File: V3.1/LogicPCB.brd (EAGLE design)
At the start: 171.9 x 151.6 mm, 65 parts, among them CON1 CUBE_ORANGE_, CON10 PINHEAD_1X02-2.54, CON11 CON-4P-JST-XA, CON12 PINHEAD_1X06-2.54, CON13 CON-6P-JST-XA, CON14 PINHEAD_1X04-2.54, CON15 CON-4P-JST-XA, CON17 CON-4P-JST-XA, CON18 CON-6P-JST-XA, CON19 USB-TYPE-C-VERT-PROD, CON2 CON-4P-JST-XA, CON20 PINHEAD_1X06-2.54, CON21 CON-4P-JST-XA, CON22 CON-4P-JST-XA, CON23 CON-4P-JST-XA, CON24 CON-4P-JST-XA, CON25 CON-4P-JST-XA, CON26 CON-4P-JST-XA, CON27 CON-4P-JST-XA, CON28 CON-4P-JST-XA, CON29 CON-4P-JST-XA, CON3 RJ45-NO_SHIELD-5556416-1, CON30 CON-4P-JST-XA, CON32 CON-4P-JST-XA, CON35 CON-12P-JST-XA, CON4 CON-2P-JST-XA, CON5 CON-6P-JST-XA, CON6 CON-4P-JST-XA, CON7 PINHEAD_1X06-2.54, CON9 PINHEAD_1X12-2.54, IC5 AOZ1280, M1 05G_ETHERNET_SWITCH, Q1 IRLML0030, T1 H1102NL, T2 H1102NL, T3 H1102NL, T4 H1102NL

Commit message: uarts
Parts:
- added R4, R5: (no value), rc:R0603
- added R6, R7: 000, rc:R0603
- moved R1 0.20 mm to (8.70, -26.3)
- moved R3 0.20 mm to (8.70, -24.7)
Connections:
- new net N$10: CON18.4, R5.1
- new net N$9: CON18.3, R4.1
- net GND: no longer CON35.10
- net HLK_RX0: now also CON35.6
- net HLK_RX1: now also R6.1
- net HLK_TX0: now also CON35.5
- net HLK_TX1: now also R7.1
- net SERIAL1_RX: now also R5.2, R7.2; no longer CON18.4
- net SERIAL1_TX: now also R4.2, R6.2; no longer CON18.3
- net SERIAL3_RX: now also CON35.8; no longer CON35.6
- net SERIAL3_TX: now also CON35.7; no longer CON35.5
- net VDD_24V: now also CON35.10; no longer CON35.7, CON35.8
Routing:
- net HLK_RX0: track 0.00 -> 81.8 mm, vias 0 -> 2
- net HLK_TX0: track 0.00 -> 76.3 mm, vias 0 -> 2
- net HLK_TX1: track 0.00 -> 43.1 mm, vias 0 -> 2
- net HLK_RX1: track 0.00 -> 39.6 mm, vias 0 -> 2
- net N$9: track 0.00 -> 13.9 mm
- net N$10: track 0.00 -> 12.1 mm
- net SERIAL1_TX: track 133.7 -> 124.0 mm
- net SERIAL1_RX: track 132.5 -> 123.1 mm
- net SERIAL3_RX: track 121.4 -> 116.5 mm
- net SERIAL3_TX: track 123.7 -> 118.8 mm
- net ETH1_RX-: track 35.4 -> 38.4 mm
- net VDD_24V: track 59.0 -> 56.5 mm
- net ETH1_RX+: track 36.6 -> 38.9 mm
- net GND: vias 114 -> 112
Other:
- board text added: "HLK0_RX"
- board text added: "HLK0_TX"
- board text added: "SER3_RX"
- board text removed: "SER_RX"

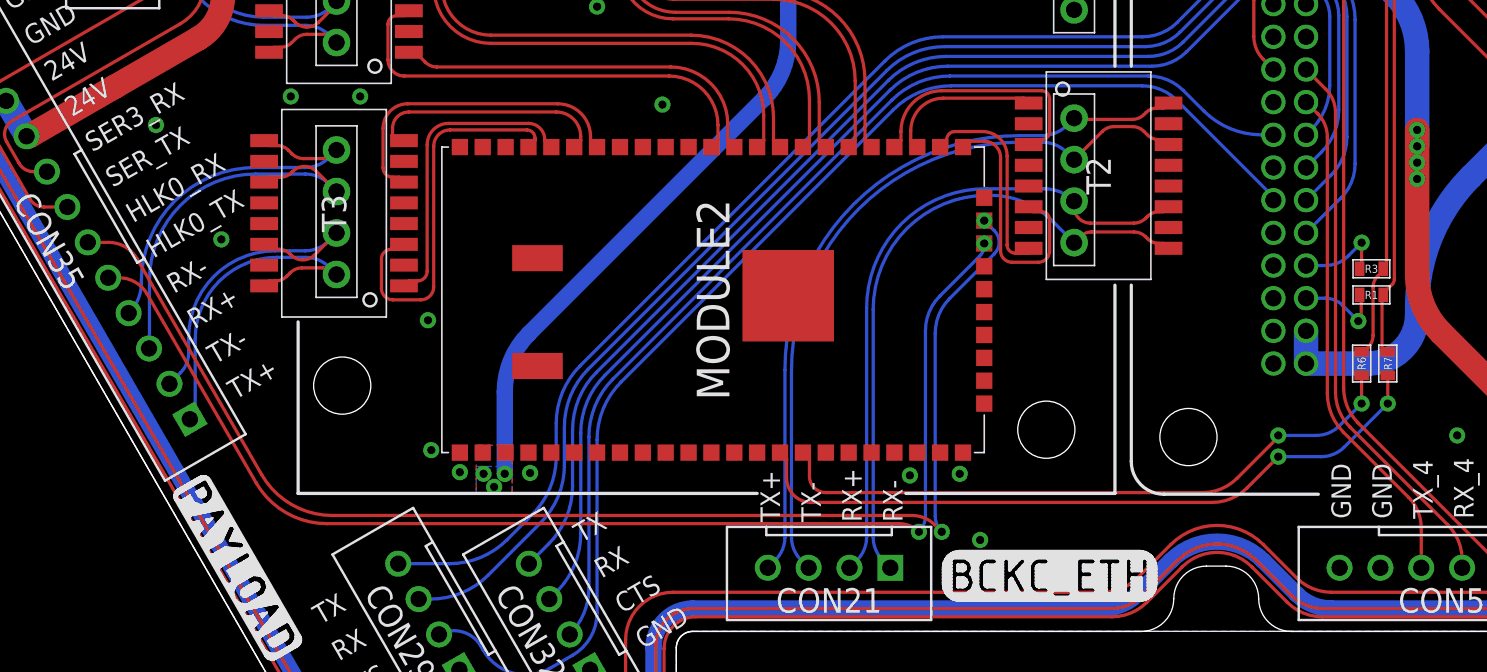
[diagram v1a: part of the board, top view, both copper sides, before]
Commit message: link leds added
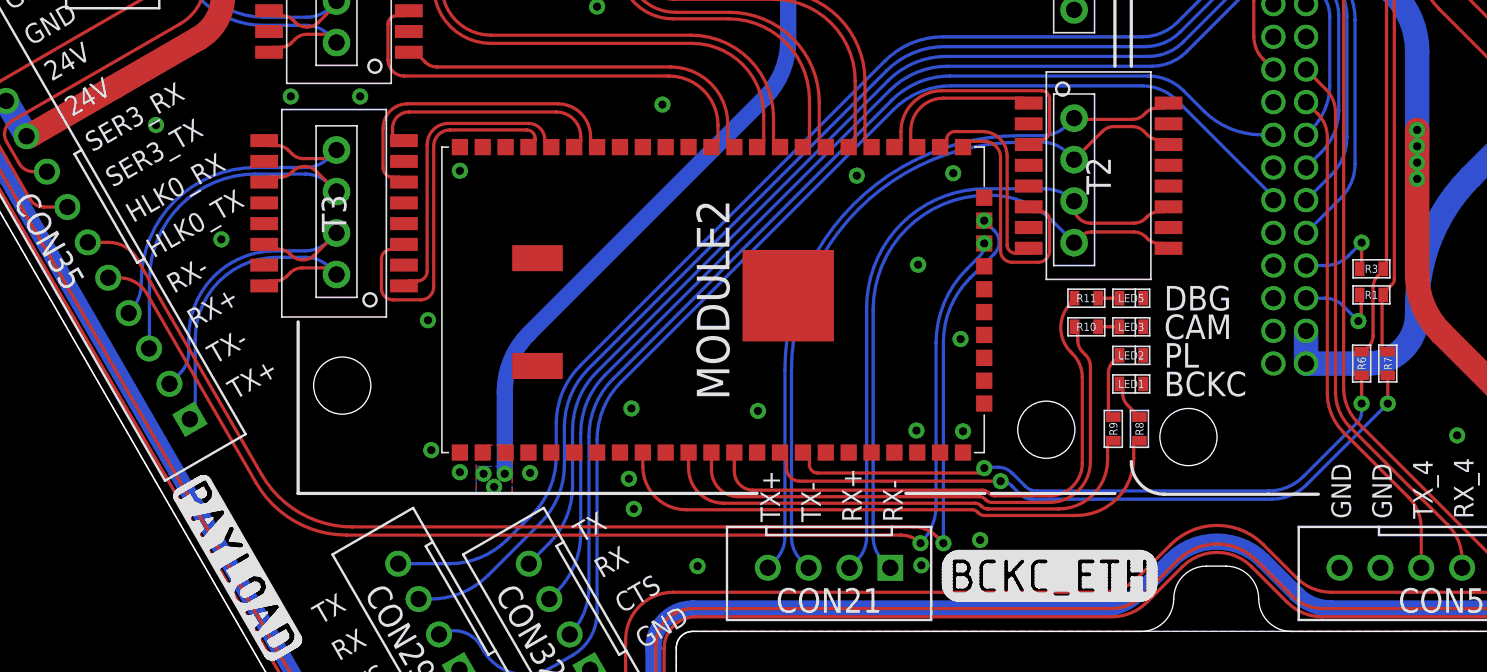
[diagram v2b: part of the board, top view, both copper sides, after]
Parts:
- added LED1, LED2, LED3, LED5: LED-0603, rc:LED0603
- added R10, R11, R8, R9: (no value), rc:R0603
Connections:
- removed net LINK0: MODULE2.13
- removed net LINK1: MODULE2.12
- new net N$11: LED1.A, R8.1
- new net N$12: LED2.A, R9.1
- new net N$14: LED3.A, R10.1
- new net N$15: LED5.A, R11.1
- new net N$16: MODULE2.12, R10.2
- new net N$17: MODULE2.13, R11.2
- net GND: now also LED1.C, LED2.C, LED3.C, LED5.C
- net LINK2: now also R9.2
- net LINK4: now also R8.2
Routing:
- net LINK4: track 0.00 -> 35.0 mm
- net N$16: track 0.00 -> 34.6 mm
- net N$17: track 0.00 -> 34.2 mm
- net LINK2: track 0.00 -> 30.3 mm
- net N$12: track 0.00 -> 4.29 mm
- net N$11: track 0.00 -> 2.47 mm
- net N$15: track 0.00 -> 1.30 mm
- net N$14: track 0.00 -> 1.30 mm
- net HLK_TX0: track 76.3 -> 76.9 mm
- net HLK_RX0: track 81.8 -> 82.4 mm
- net HLK_TX1: track 43.1 -> 42.5 mm
- net GND: vias 112 -> 123
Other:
- board text added: "BCKC"
- board text added: "CAM"
- board text added: "DBG"
- board text added: "PL"
- board text added: "SER3_TX"
- board text removed: "SER_TX"

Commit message: Naming
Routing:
- net BATT_CURRENT: track 54.9 -> 56.0 mm
- net SERIAL1_RX: track 123.1 -> 122.4 mm
- net SERIAL1_TX: track 124.0 -> 123.3 mm
- net ALARM: track 33.9 -> 34.5 mm
- net GND: vias 123 -> 126

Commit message: attribute updates
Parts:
- added D2, D3: ESDA5V3L, TVS_diodes:SOT23B-3
- added PAD1, PAD2: PAD-HEX-2MM, PADS:HEX-2MM
- added R12, R14, R15: 120R, rc:R0603
- D1: value MBR0520L-SOD123 -> SS34; device Diodes:SOD123 -> Diodes:DO-214AC(SMA)
- R1, R3, R6, R7: value 000 -> 120R
- R10, R11, R8, R9: value (none) -> 1K
- R16: value 10K -> 51K
- R20: value 200R -> 120R
- R35, R36, R37, R38: value 100R -> 120R
- R4, R5: value (none) -> 120R
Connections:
- new net N$18: CON18.5, R12.1
- net GND: now also D2.3, D3.3
- net HLK_RX0: now also R14.1
- net HLK_TX0: now also R15.1
- net PPM-SBUS-PROT: now also D3.1, R12.2; no longer CON18.5
- net RX_2: now also R14.2
- net SERIAL1_RX: now also D2.1
- net SERIAL1_TX: now also D2.2
- net TX_2: now also R15.2
- net USB_DM: now also PAD2.1
- net USB_DP: now also PAD1.1
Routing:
- net N$18: track 0.00 -> 10.4 mm
- net PPM-SBUS-PROT: track 81.2 -> 71.0 mm
- net RX_2: track 88.6 -> 98.1 mm
- net TX_2: track 91.9 -> 99.8 mm
- net USB_DP: track 0.00 -> 2.52 mm, vias 0 -> 1
- net USB_DM: track 0.00 -> 2.52 mm, vias 0 -> 1
- net HLK_TX0: track 76.9 -> 76.3 mm
- net HLK_RX0: track 82.4 -> 81.8 mm
- net GND: vias 126 -> 128
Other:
- board text added: "CON200"

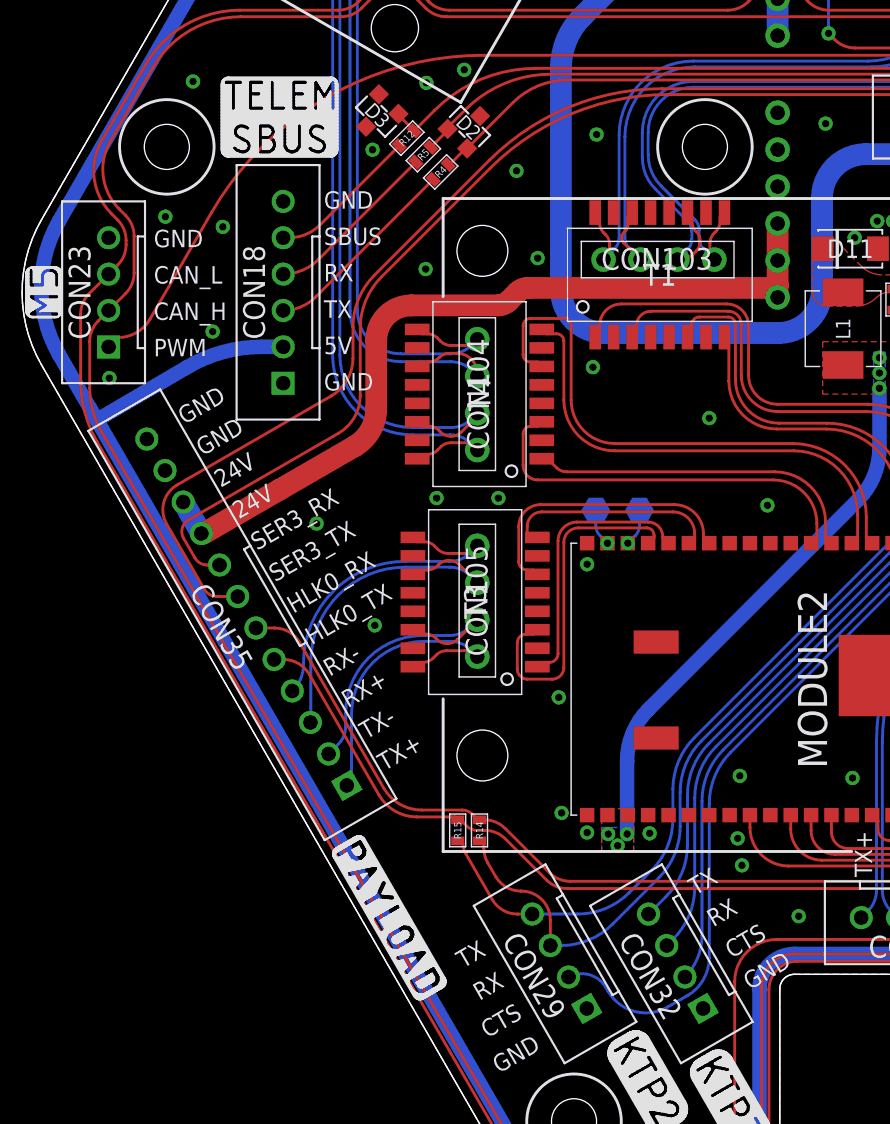
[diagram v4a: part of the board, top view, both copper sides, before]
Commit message: Payload connector replaced with 2 6-pin ones
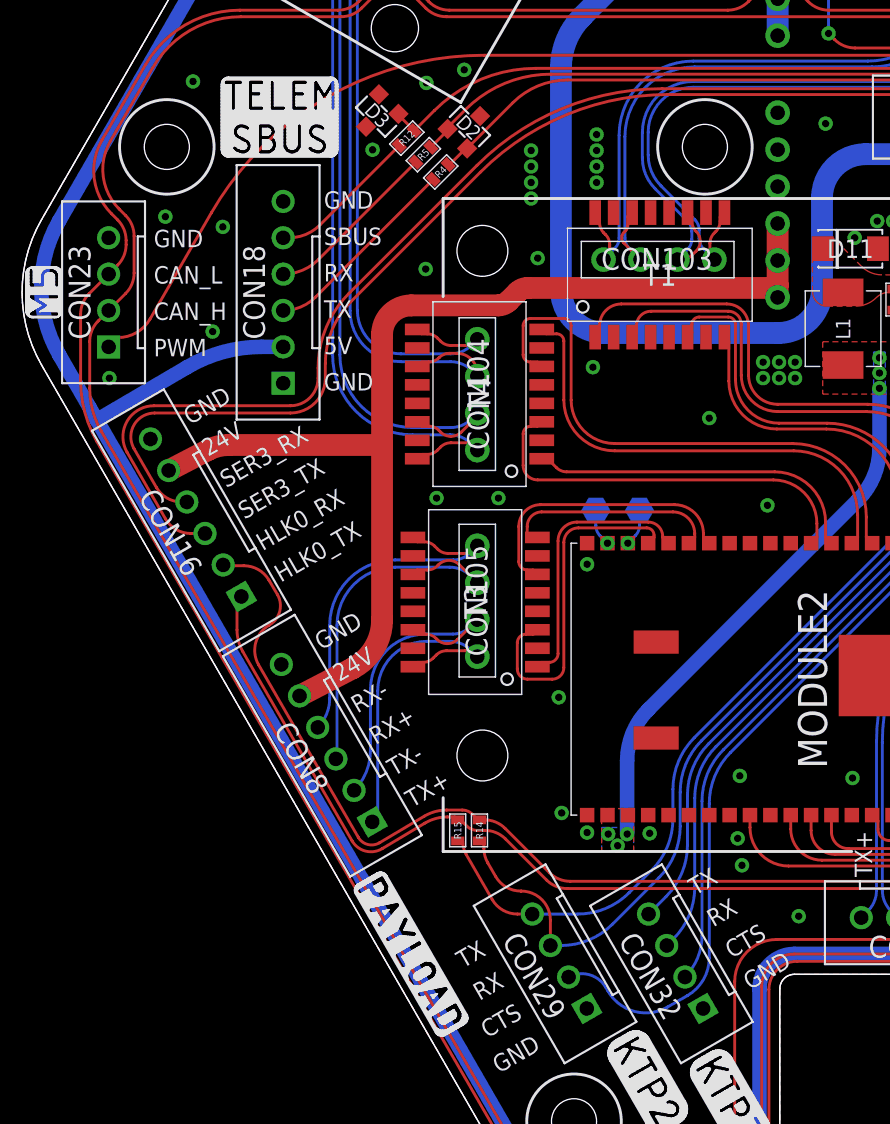
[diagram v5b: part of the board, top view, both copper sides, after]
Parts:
- removed CON35: CON-12P-JST-XA, Connectors:B12B-XASK-1
- added CON16, CON8: CON-6P-JST-XA, Connectors:B06B-XASK-1
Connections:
- net ETH5_RX+: now also CON8.3; no longer CON35.3
- net ETH5_RX-: now also CON8.4; no longer CON35.4
- net ETH5_TX+: now also CON8.1; no longer CON35.1
- net ETH5_TX-: now also CON8.2; no longer CON35.2
- net GND: now also CON16.6, CON8.6; no longer CON35.11, CON35.12
- net HLK_RX0: now also CON16.2; no longer CON35.6
- net HLK_TX0: now also CON16.1; no longer CON35.5
- net SERIAL3_RX: now also CON16.4; no longer CON35.8
- net SERIAL3_TX: now also CON16.3; no longer CON35.7
- net VDD_24V: now also CON16.5, CON8.5; no longer CON35.10, CON35.9
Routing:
- net VDD_24V: track 56.5 -> 76.3 mm
- net HLK_RX0: track 81.8 -> 92.2 mm
- net HLK_TX0: track 76.3 -> 85.1 mm
- net ETH5_RX-: track 22.2 -> 24.4 mm
- net ETH5_RX+: track 23.8 -> 26.0 mm
- net ETH5_TX+: track 20.9 -> 22.6 mm
- net ETH5_TX-: track 20.0 -> 21.6 mm
- net SERIAL3_RX: track 116.8 -> 118.1 mm
- net SERIAL3_TX: track 119.0 -> 119.9 mm
- net GND: vias 128 -> 138

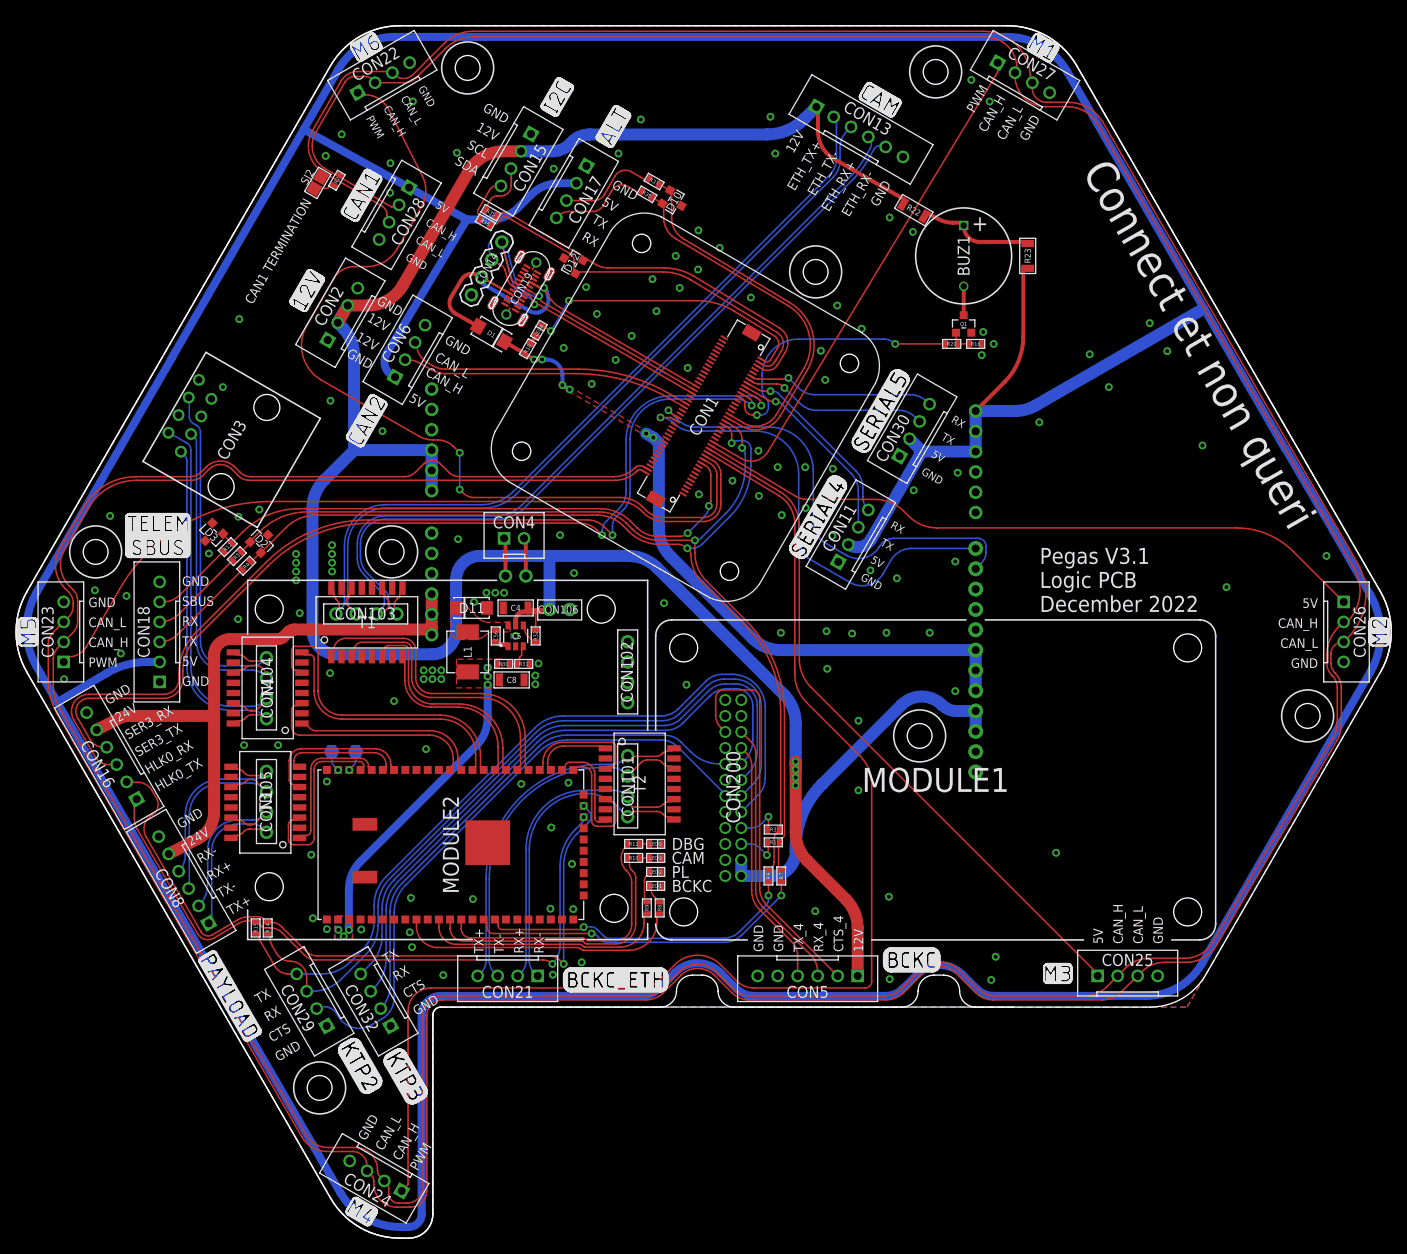
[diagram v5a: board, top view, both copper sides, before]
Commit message: InterPCB connectors issues fix
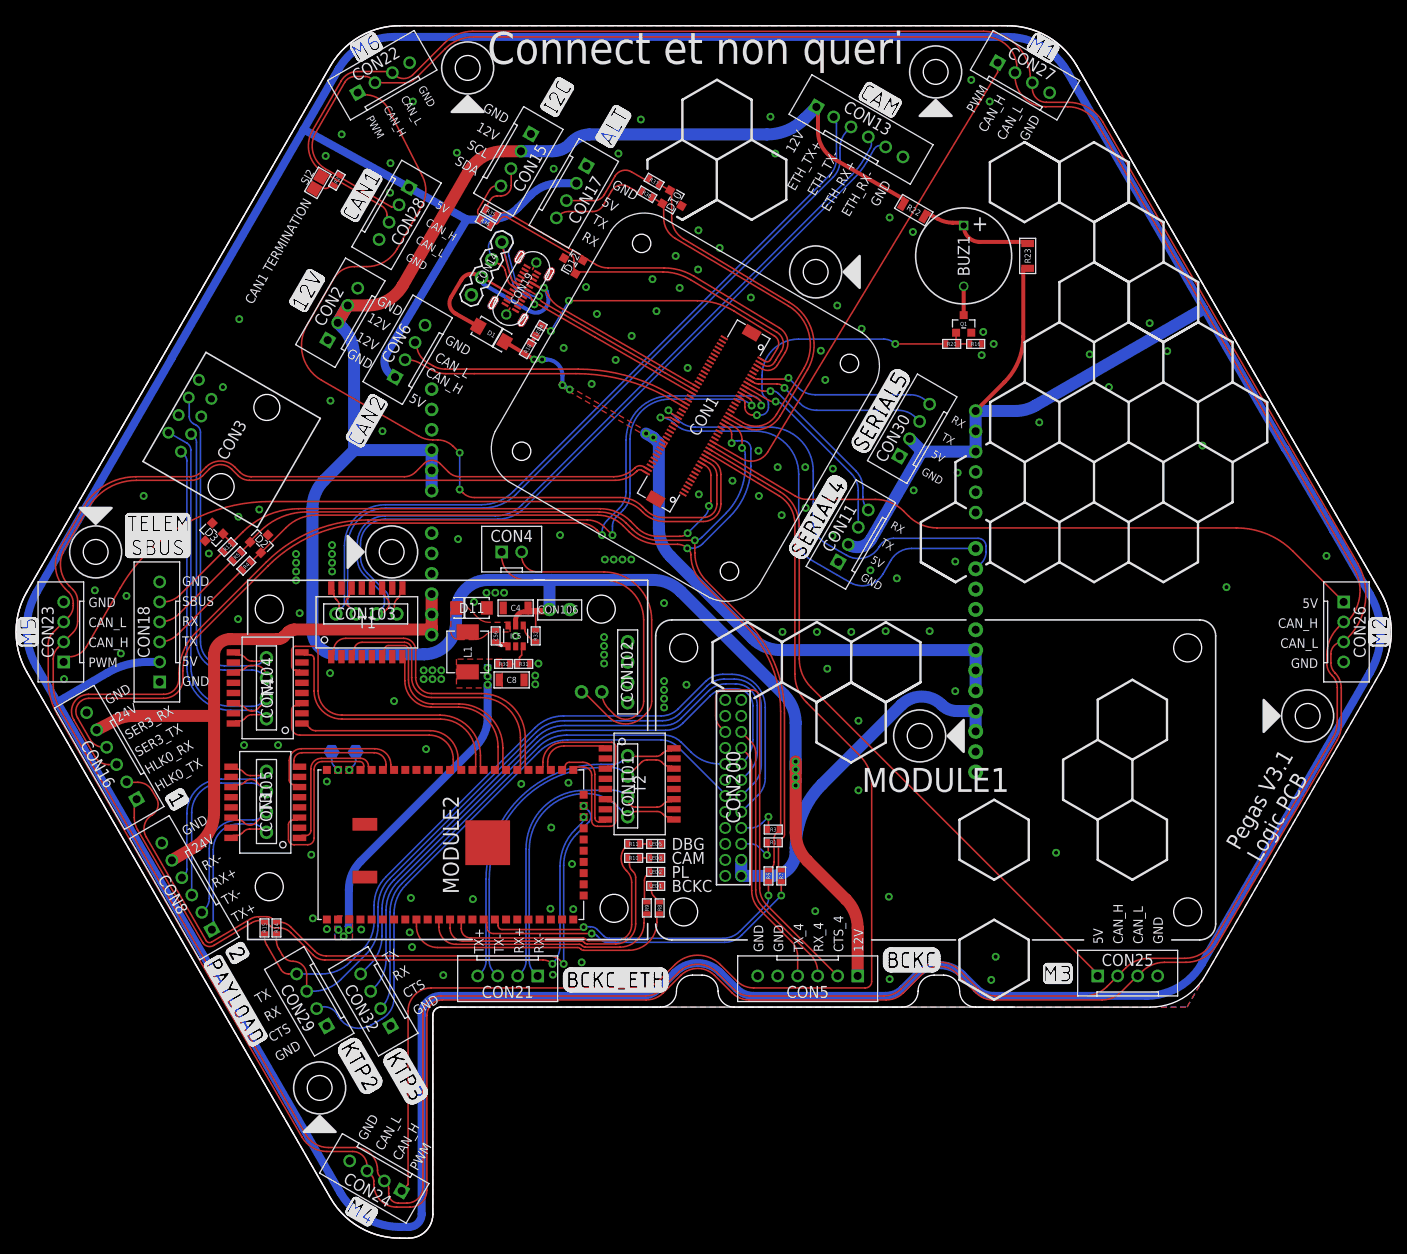
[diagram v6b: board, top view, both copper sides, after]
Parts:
- moved CON10 17.3 mm to (-14.0, -7.50), turned to 0 degrees
- moved CON4 1.73 mm to (-24.0, 10.0)
- moved R14 1.10 mm to (-53.4, -37.0)
- moved R15 1.10 mm to (-54.9, -37.0)
- moved CON8 0.89 mm to (-64.6, -31.8)
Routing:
- net N$7: track 4.79 -> 41.5 mm
- net N$2: track 4.77 -> 39.7 mm
- net VDD_12V: track 278.3 -> 270.0 mm
- net HLK_TX0: track 85.1 -> 86.0 mm
- net HLK_RX0: track 92.2 -> 93.1 mm
- net TX_2: track 99.8 -> 99.0 mm
- net ETH5_TX-: track 21.6 -> 22.4 mm
- net ETH5_RX-: track 24.4 -> 25.2 mm
- net RX_2: track 98.1 -> 97.4 mm
- net ETH5_RX+: track 26.0 -> 26.7 mm
- net ETH5_TX+: track 22.6 -> 23.2 mm
- net GND: vias 138 -> 149
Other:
- board text added: "DM"
- board text added: "DP"
- board text added: "December 2022"
- board text added: "Pegas V3.1 Logic PCB"
- board text removed: "Pegas V3.1 Logic PCB December 2022"

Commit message: silk updates
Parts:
- moved R8 2.75 mm to (-6.00, -37.2)
- moved R9 0.50 mm to (-6.80, -34.1)
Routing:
- net LINK4: track 35.0 -> 32.5 mm
- net N$11: track 2.47 -> 4.96 mm
- net N$16: track 34.6 -> 35.6 mm
- net N$17: track 34.2 -> 35.2 mm
- net LINK2: track 30.3 -> 30.9 mm

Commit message: Minor fixes here and there
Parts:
- moved CON2 0.86 mm to (-45.5, 40.5), turned to 240 degrees
- moved CON6 0.50 mm to (-37.0, 35.5), turned to 240 degrees
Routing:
- net VDD_5V: track 678.7 -> 670.3 mm
- net CAN2_L: track 36.2 -> 39.9 mm
- net VDD_12V: track 270.0 -> 268.4 mm
- net GND: vias 149 -> 152
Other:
- board text added: "11 mm female to female M3 standoffs"
- board text added: "8 mm female to female M3 standoffs"
- board text added: "CANH"
- board text added: "CANL"
- board text added: "Use M3 ISO7380 screws for everything"
- board text removed: "CAN_H"
- board text removed: "CAN_L"
